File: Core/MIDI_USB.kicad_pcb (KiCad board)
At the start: 4 copper layers, 37.8 x 99.8 mm, 102 parts, among them J1 Conn_01x04, J10 AudioJack3_SwitchTR, J4 Conn_01x06, J5 USB_C_Receptacle_USB2.0, J6 Conn_02x08_Odd_Even, J7 AudioJack3_SwitchTR, J8 AudioJack3_SwitchTR, J9 AudioJack3_SwitchTR, Q3 SQ2361, Q4 2N7002, SW1 SW_Push_DPDT, U1 ATSAMD21G15B-A, U10 TLE9250V, U2 MIC2005-2YM5, U3 TUSB320, U4 TL072, U5 MIC5504-3.3YM5, U6 ES9023P, U7 PCM1808, U8 TL072, U9 MCP2517FD-xSL, Y1 20MHz

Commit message: Fix symbols
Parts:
- C35: value 22nF -> 4.7nF
- R28: value 10k -> 1k
- R4, R5: value 120 -> 56

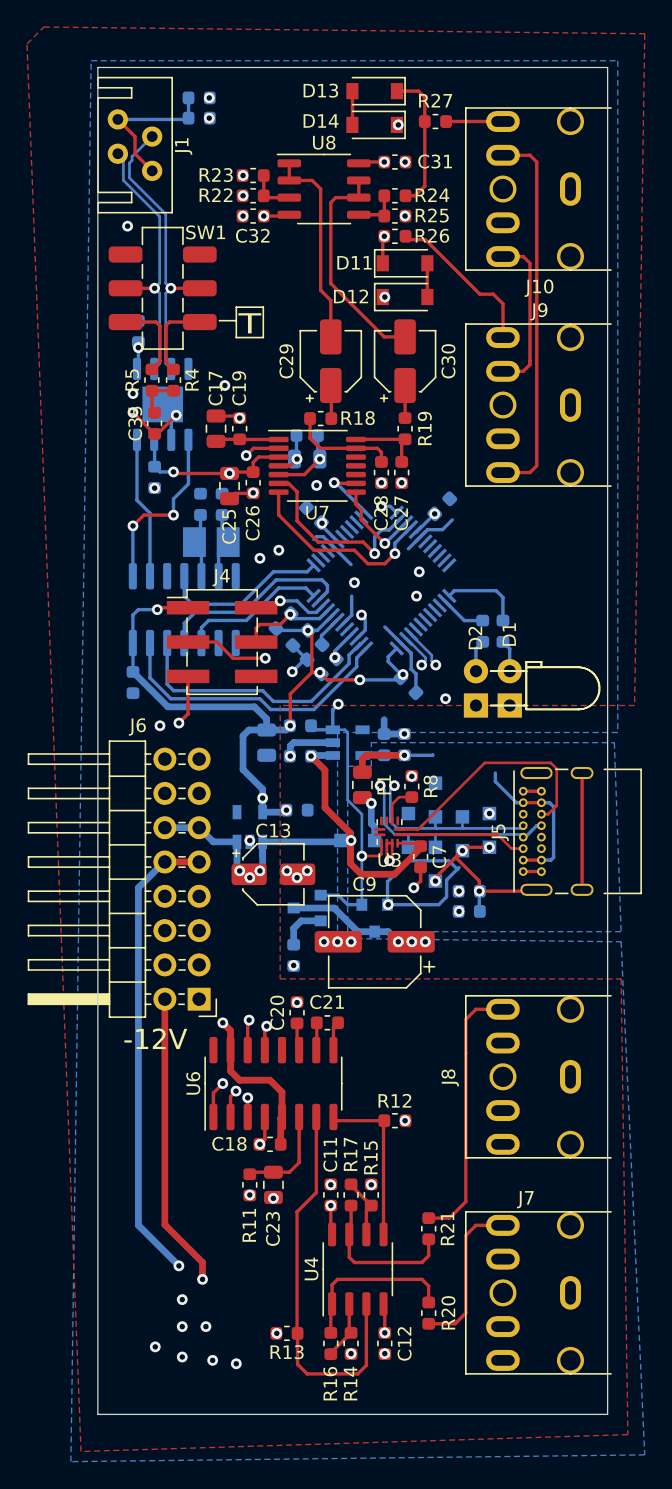
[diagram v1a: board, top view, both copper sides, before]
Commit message: Add custom footprints
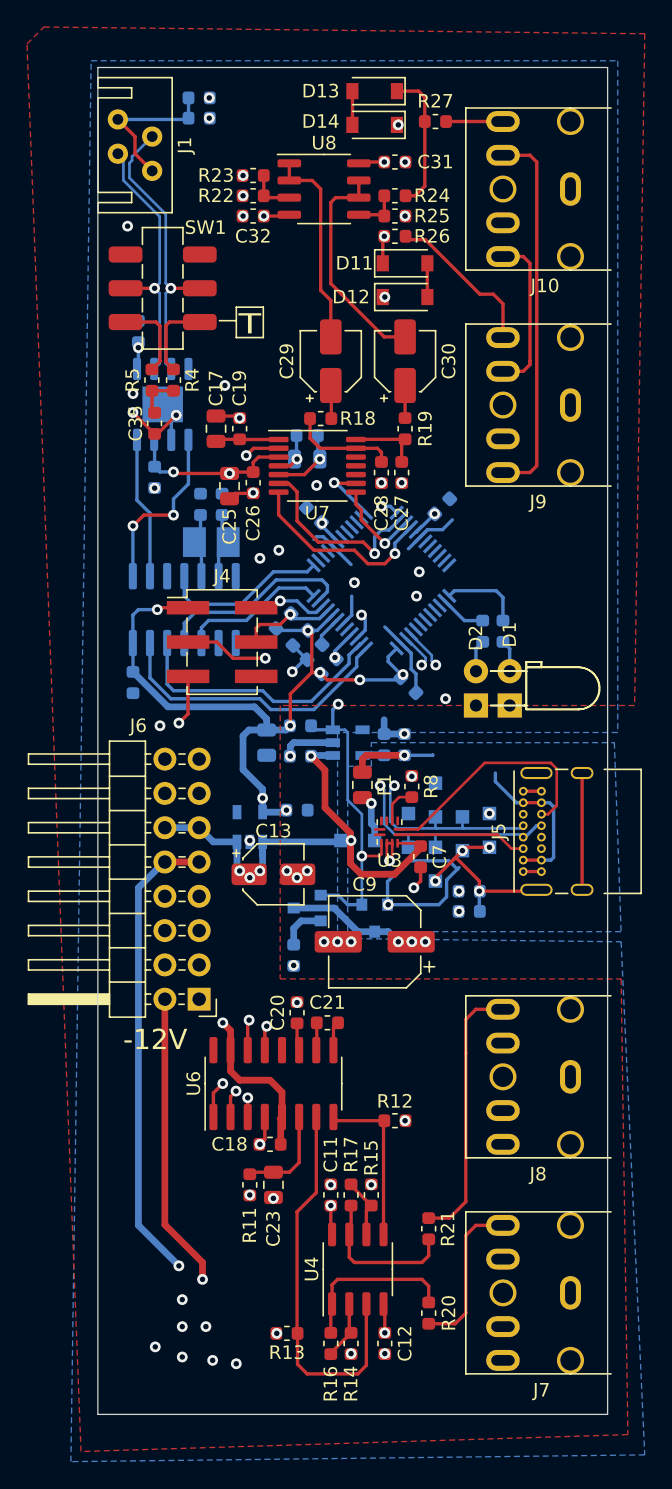
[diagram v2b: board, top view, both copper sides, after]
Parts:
- J1: footprint CustomLib:MicroMatch_04_Angled -> Custom_FP:MicroMatch_04_Angled
- J10, J7, J8, J9: footprint CustomLib:STX3100_Angled_3.5mm -> Custom_FP:STX3100_Angled_3.5mm
- J5: footprint CustomLib:USB_C_Receptacle_GCT_USB4085_Slimmed -> Custom_FP:USB_C_Receptacle_GCT_USB4085_Slimmed
- SW1: footprint CustomLib:SlideDPDT_JS202011 -> Custom_FP:SlideDPDT_JS202011
- Y1: footprint CustomLib:Crystal_2pin_2.0x2.5mm -> Custom_FP:Crystal_2pin_2.0x2.5mm
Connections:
- J10 pad RN: (no net) -> Net-(J10-PadRN)
- J4 pad 6: (no net) -> Net-(J4-Pad6)
- J5 pad A8: (no net) -> Net-(J5-PadA8)
- J5 pad B8: (no net) -> Net-(J5-PadB8)
- J6 pad 13: (no net) -> Net-(J6-Pad13)
- J6 pad 14: (no net) -> Net-(J6-Pad14)
- J6 pad 15: (no net) -> Net-(J6-Pad15)
- J6 pad 16: (no net) -> Net-(J6-Pad16)
- J7 pad R: (no net) -> Net-(J7-PadR)
- J7 pad RN: (no net) -> Net-(J7-PadRN)
- J7 pad TN: (no net) -> Net-(J7-PadTN)
- J8 pad R: (no net) -> Net-(J8-PadR)
- J8 pad RN: (no net) -> Net-(J8-PadRN)
- J8 pad TN: (no net) -> Net-(J8-PadTN)
- J9 pad RN: (no net) -> Net-(J9-PadRN)
- SW1 pad 3: (no net) -> Net-(SW1-Pad3)
- SW1 pad 6: (no net) -> Net-(SW1-Pad6)
- U1 pad 10: (no net) -> Net-(U1-Pad10)
- U1 pad 11: (no net) -> Net-(U1-Pad11)
- U1 pad 19: (no net) -> Net-(U1-Pad19)
- U1 pad 2: (no net) -> Net-(U1-Pad2)
- U1 pad 20: (no net) -> Net-(U1-Pad20)
- U1 pad 21: (no net) -> Net-(U1-Pad21)
- U1 pad 22: (no net) -> Net-(U1-Pad22)
- U1 pad 23: (no net) -> Net-(U1-Pad23)
- U1 pad 24: (no net) -> Net-(U1-Pad24)
- U1 pad 27: (no net) -> Net-(U1-Pad27)
- U1 pad 28: (no net) -> Net-(U1-Pad28)
- U1 pad 29: (no net) -> Net-(U1-Pad29)
- U1 pad 3: (no net) -> Net-(U1-Pad3)
- U1 pad 30: (no net) -> Net-(U1-Pad30)
- U1 pad 31: (no net) -> Net-(U1-Pad31)
- U1 pad 32: (no net) -> Net-(U1-Pad32)
- U1 pad 4: (no net) -> Net-(U1-Pad4)
- U1 pad 41: (no net) -> Net-(U1-Pad41)
- U1 pad 7: (no net) -> Net-(U1-Pad7)
- U1 pad 8: (no net) -> Net-(U1-Pad8)
- U1 pad 9: (no net) -> Net-(U1-Pad9)
- U2 pad 4: (no net) -> Net-(U2-Pad4)
- U3 pad 3: (no net) -> Net-(U3-Pad3)
- U3 pad 5: (no net) -> Net-(U3-Pad5)
- U3 pad 6: (no net) -> Net-(U3-Pad6)
- U3 pad 7: (no net) -> Net-(U3-Pad7)
- U3 pad 8: (no net) -> Net-(U3-Pad8)
- U5 pad 4: (no net) -> Net-(U5-Pad4)
- U6 pad 16: (no net) -> Net-(U6-Pad16)
- U7 pad 10: (no net) -> Net-(U7-Pad10)
- U7 pad 11: (no net) -> Net-(U7-Pad11)
- U7 pad 12: (no net) -> Net-(U7-Pad12)
- U9 pad 3: (no net) -> Net-(U9-Pad3)
- U9 pad 8: (no net) -> Net-(U9-Pad8)
- U9 pad 9: (no net) -> Net-(U9-Pad9)

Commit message: Update to v1.1
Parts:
- removed C13: 3.3µF, Capacitor_SMD:CP_Elec_4x5.4
- removed C8: 1µF, Capacitor_SMD:C_0603_1608Metric
- removed C9: 120µF, Capacitor_SMD:CP_Elec_6.3x5.7
- removed D13, D14: 5V6, Diode_SMD:D_SOD-123
- removed F1: PSMF020X-2, Fuse:Fuse_0805_2012Metric
- removed Q4: 2N7002, Package_TO_SOT_SMD:SOT-23
- removed R27: 1k, Resistor_SMD:R_0603_1608Metric
- removed U2: MIC2005-2YM5, Package_TO_SOT_SMD:SOT-23-5
- removed U3: TUSB320, Package_DFN_QFN:Texas_X2QFN-12_1.6x1.6mm_P0.4mm
- added C39: 100nF, Capacitor_SMD:C_0603_1608Metric, B.Cu at (150.2, 99.7)
- added C40: 100nF, Capacitor_SMD:C_0603_1608Metric, B.Cu at (157.2, 99.6)
- added C41: 15pF, Capacitor_SMD:C_0603_1608Metric, B.Cu at (148.6, 120.6)
- added C42: 15pF, Capacitor_SMD:C_0603_1608Metric, B.Cu at (146.4, 122.8)
- added C43: 1µF, Capacitor_SMD:C_0603_1608Metric, F.Cu at (158.0, 141.2)
- added C44: 47µF, Capacitor_SMD:C_1210_3225Metric, F.Cu at (151.8, 141.8)
- added C45: 47µF, Capacitor_SMD:C_1210_3225Metric, F.Cu at (151.8, 145.0)
- added C46: 47µF, Capacitor_SMD:C_1210_3225Metric, F.Cu at (151.8, 148.2)
- added D3: SD103, Diode_SMD:D_SOD-323_HandSoldering, F.Cu at (152.0, 112.8)
- added D4: SD103, Diode_SMD:D_SOD-323_HandSoldering, F.Cu at (150.0, 112.8)
- added Q1: ZXMP3A13, Package_TO_SOT_SMD:SOT-23, B.Cu at (144.8, 152.0)
- added Q2: PMV88ENER, Package_TO_SOT_SMD:SOT-23, B.Cu at (145.2, 159.5)
- added Q5: ZXMP3A13, Package_TO_SOT_SMD:SOT-23, B.Cu at (144.8, 148.0)
- added Q6: MMBT3904, Package_TO_SOT_SMD:SOT-23, B.Cu at (148.8, 152.5)
- added R29: 1M, Resistor_SMD:R_0603_1608Metric, B.Cu at (151.5, 154.5)
- added R30: 100k, Resistor_SMD:R_0603_1608Metric, B.Cu at (149.0, 149.5)
- added SW2: SW_SPST, Button_Switch_THT:SW_Tactile_SPST_Angled_PTS645Vx58-2LFS, F.Cu at (167.8, 124.9)
- added SW4: SW_SPST, Button_Switch_SMD:SW_SPST_B3U-1000P, F.Cu at (140.3, 126.7)
- added U11: CAT250640VI, Package_SO:SOIC-8_3.9x4.9mm_P1.27mm, B.Cu at (148.2, 105.0)
- added U12: APS1604M, Package_SO:SOIC-8_3.9x4.9mm_P1.27mm, B.Cu at (155.2, 105.0)
- added U13: ~, Package_SON:WSON-12-1EP_3x2mm_P0.5mm_EP1x2.65, F.Cu at (157.2, 144.1)
- added Y2: 32.768kHz, Crystal:Crystal_SMD_EuroQuartz_EQ161-2Pin_3.2x1.5mm_HandSoldering, B.Cu at (149.0, 123.2)
- C22, C24, R28: moved to F.Cu
- C29, C30: value 1µF -> 10µF bi-polar; footprint Capacitor_SMD:CP_Elec_4x5.4 -> Capacitor_SMD:CP_Elec_5x5.8
- D11, D12: value 5V6 -> SD103; footprint Diode_SMD:D_SOD-123 -> Diode_SMD:D_SOD-323_HandSoldering
- J5: footprint Custom_FP:USB_C_Receptacle_GCT_USB4085_Slimmed -> Connector_USB:USB_C_Receptacle_HRO_TYPE-C-31-M-12
- Q3: value SQ2361 -> MMBT3904
- R16, R17: value 42k -> 27k
- R26: value 1k -> 10k; moved to B.Cu
- R4, R5: value 56 -> 62
- R6: value 10k -> 100k; moved to F.Cu
- R8: value 910k -> 100k
- R9: value 470 -> 100k
- U1: value ATSAMD21G15B-A -> ATSAMD21G17D-A
- moved R26 19.7 mm to (161.0, 121.5), turned to -135 degrees
- moved R9 16.2 mm to (154.2, 141.2), turned to 0 degrees
- moved Q3 14.8 mm to (152.2, 138.5), turned to 90 degrees
- moved C20 12.0 mm to (158.0, 166.5), turned to 0 degrees
- moved C21 10.6 mm to (157.2, 168.8), turned to 90 degrees
- moved R6 9.22 mm to (155.0, 145.0), turned to -90 degrees
- moved D11 8.10 mm to (154.5, 112.8), turned to 90 degrees
- moved R22 7.28 mm to (146.5, 92.8), turned to 180 degrees
- moved R19 7.02 mm to (155.2, 110.0), turned to 180 degrees
- moved C7 6.96 mm to (155.0, 142.0), turned to 90 degrees
- moved U6 6.82 mm to (152.8, 164.5), turned to 0 degrees
- moved C30 6.77 mm to (156.2, 105.2)
- moved C29 6.75 mm to (150.2, 105.2)
- moved R18 6.49 mm to (151.2, 110.0), turned to 0 degrees
- moved C23 6.39 mm to (147.3, 166.8), turned to 180 degrees
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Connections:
- net MIDIBUS+ renamed M2IDI+
- net MIDIBUS- renamed M2IDI-
- net Net-(U1-Pad41) renamed PROG
- net SPI_SS renamed CAN_SS
- C11 pad 2: GNDA -> GND
- C12 pad 1: GNDA -> GND
- C17 pad 2: GNDA -> GND
- C18 pad 2: GNDA -> GND
- C19 pad 2: GNDA -> GND
- C20 pad 2: GNDA -> GND
- C23 pad 2: GNDA -> GND
- C25 pad 2: GNDA -> GND
- C26 pad 2: GNDA -> GND
- C27 pad 1: Net-(C27-Pad1) -> Net-(D11-A)
- C27 pad 2: GNDA -> GND
- C28 pad 2: GNDA -> GND
- C31 pad 2: GNDA -> GND
- C32 pad 1: GNDA -> GND
- D10 pad 2: Net-(D10-Pad2) -> VBUS
- D11 pad 1: Net-(D11-Pad1) -> +5V
- D11 pad 2: Net-(D11-Pad2) -> Net-(D11-A)
- D12 pad 1: GNDA -> Net-(D11-A)
- D12 pad 2: Net-(D11-Pad2) -> GND
- J10 pad RN: Net-(J10-PadRN) -> unconnected-(J10-PadRN)
- J10 pad S: GNDA -> GND
- J10 pad TN: Net-(J10-PadTN) -> unconnected-(J10-PadTN)
- J4 pad 6: Net-(J4-Pad6) -> unconnected-(J4-Pin_6-Pad6)
- J5 pad A8: Net-(J5-PadA8) -> unconnected-(J5-SBU1-PadA8)
- J5 pad B8: Net-(J5-PadB8) -> unconnected-(J5-SBU2-PadB8)
- J6 pad 1: -VDC -> Net-(J6-Pin_1)
- J6 pad 10: +VDC -> Net-(J6-Pin_10)
- J6 pad 11: +5V -> Net-(J6-Pin_11)
- J6 pad 12: +5V -> Net-(J6-Pin_11)
- J6 pad 13: Net-(J6-Pad13) -> unconnected-(J6-Pin_13-Pad13)
- J6 pad 14: Net-(J6-Pad14) -> unconnected-(J6-Pin_14-Pad14)
- J6 pad 15: Net-(J6-Pad15) -> unconnected-(J6-Pin_15-Pad15)
- J6 pad 16: Net-(J6-Pad16) -> unconnected-(J6-Pin_16-Pad16)
- J6 pad 2: -VDC -> Net-(J6-Pin_1)
- J6 pad 5: GNDA -> GND
- J6 pad 6: GNDA -> GND
- J6 pad 9: +VDC -> Net-(J6-Pin_10)
- J7 pad R: Net-(J7-PadR) -> unconnected-(J7-PadR)
- J7 pad RN: Net-(J7-PadRN) -> unconnected-(J7-PadRN)
- J7 pad S: GNDA -> GND
- J7 pad TN: Net-(J7-PadTN) -> unconnected-(J7-PadTN)
- J8 pad R: Net-(J8-PadR) -> unconnected-(J8-PadR)
- J8 pad RN: Net-(J8-PadRN) -> unconnected-(J8-PadRN)
- J8 pad S: GNDA -> GND
- J8 pad TN: Net-(J8-PadTN) -> unconnected-(J8-PadTN)
- J9 pad R: Net-(J10-PadTN) -> unconnected-(J9-PadR)
- J9 pad RN: Net-(J9-PadRN) -> unconnected-(J9-PadRN)
- J9 pad S: GNDA -> GND
- Q3 pad 1: USB_ID -> Net-(Q3-B)
- Q3 pad 2: VBUS -> GND
- Q3 pad 3: Net-(C9-Pad1) -> Net-(Q3-C)
- R11 pad 2: GNDA -> GND
- R12 pad 2: GNDA -> GND
- R13 pad 2: GNDA -> GND
- R14 pad 2: GNDA -> GND
- R15 pad 2: GNDA -> GND
- R19 pad 2: Net-(C27-Pad1) -> Net-(D11-A)
- R22 pad 1: Net-(D11-Pad1) -> Net-(J9-PadT)
- R22 pad 2: Net-(R22-Pad2) -> Net-(U8A--)
- R23 pad 1: Net-(R22-Pad2) -> Net-(U8A--)
- R23 pad 2: GNDA -> Net-(C29-Pad2)
- R24 pad 1: Net-(D13-Pad1) -> Net-(J10-PadT)
- R24 pad 2: Net-(R24-Pad2) -> Net-(U8B--)
- R25 pad 1: Net-(R24-Pad2) -> Net-(U8B--)
- R25 pad 2: GNDA -> Net-(C30-Pad2)
- R26 pad 1: Net-(J9-PadT) -> +3V3
- R26 pad 2: Net-(D11-Pad1) -> IO_BUTT
- R6 pad 1: +3V3 -> +5V
- R7 pad 1: VBUS -> +3V3
- R7 pad 2: GND -> Net-(Q3-C)
- R8 pad 1: VBUS -> Net-(U13-REF)
- R8 pad 2: Net-(R8-Pad2) -> GND
- R9 pad 1: Net-(Q4-Pad2) -> Net-(Q3-B)
- R9 pad 2: GND -> USB_ID
- SW1 pad 3: Net-(SW1-Pad3) -> unconnected-(SW1-C-Pad3)
- SW1 pad 6: Net-(SW1-Pad6) -> unconnected-(SW1-C-Pad6)
- U1 pad 1: CAN_INT -> Net-(U1-PA00)
- U1 pad 10: Net-(U1-Pad10) -> unconnected-(U1-PA05-Pad10)
- U1 pad 11: Net-(U1-Pad11) -> EEPROM_SS
- U1 pad 19: Net-(U1-Pad19) -> unconnected-(U1-PB10-Pad19)
- U1 pad 20: Net-(U1-Pad20) -> IO_BUTT
- U1 pad 21: Net-(U1-Pad21) -> SPI2_MOSI
- U1 pad 22: Net-(U1-Pad22) -> SPI2_SCK
- U1 pad 23: Net-(U1-Pad23) -> RAM_SS
- U1 pad 24: Net-(U1-Pad24) -> SPI2_MISO
- U1 pad 27: Net-(U1-Pad27) -> unconnected-(U1-PA18-Pad27)
- U1 pad 28: Net-(U1-Pad28) -> unconnected-(U1-PA19-Pad28)
- U1 pad 29: Net-(U1-Pad29) -> unconnected-(U1-PA20-Pad29)
- U1 pad 3: Net-(U1-Pad3) -> CAN_INT
- U1 pad 30: Net-(U1-Pad30) -> unconnected-(U1-PA21-Pad30)
- U1 pad 31: Net-(U1-Pad31) -> unconnected-(U1-PA22-Pad31)
- U1 pad 32: Net-(U1-Pad32) -> unconnected-(U1-PA23-Pad32)
- U1 pad 39: USB_ID -> Net-(Q3-C)
- U1 pad 4: Net-(U1-Pad4) -> unconnected-(U1-PA03-Pad4)
- U1 pad 7: Net-(U1-Pad7) -> unconnected-(U1-PB08-Pad7)
- U1 pad 8: Net-(U1-Pad8) -> unconnected-(U1-PB09-Pad8)
- U1 pad 9: Net-(U1-Pad9) -> unconnected-(U1-PA04-Pad9)
- U5 pad 4: Net-(U5-Pad4) -> unconnected-(U5-NC-Pad4)
- U6 pad 12: GNDA -> GND
- U6 pad 16: Net-(U6-Pad16) -> unconnected-(U6-ZD-Pad16)
- U6 pad 4: GNDA -> GND
- U7 pad 10: Net-(U7-Pad10) -> unconnected-(U7-MD0-Pad10)
- U7 pad 11: Net-(U7-Pad11) -> unconnected-(U7-MD1-Pad11)
- U7 pad 12: Net-(U7-Pad12) -> unconnected-(U7-FMT-Pad12)
- U7 pad 14: Net-(C27-Pad1) -> Net-(D11-A)
- U7 pad 2: GNDA -> GND
- U8 pad 2: Net-(C29-Pad2) -> Net-(U8A--)
- U8 pad 3: Net-(R22-Pad2) -> GND
- U8 pad 5: Net-(R24-Pad2) -> GND
- U8 pad 6: Net-(C30-Pad2) -> Net-(U8B--)
- U9 pad 3: Net-(U9-Pad3) -> unconnected-(U9-CLKO/SOF-Pad3)
- U9 pad 8: Net-(U9-Pad8) -> unconnected-(U9-~{INT1}/GPIO1-Pad8)
- U9 pad 9: Net-(U9-Pad9) -> unconnected-(U9-~{INT0}/GPIO0/XSTBY-Pad9)
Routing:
- net +3V3: track 166.5 -> 230.1 mm, vias 13 -> 17
- net SPI2_MISO: track 0.00 -> 39.8 mm, vias 0 -> 2
- net SPI2_SCK: track 0.00 -> 39.4 mm
- net SPI2_MOSI: track 0.00 -> 37.4 mm
- net Net-(J10-PadTN): track 27.9 -> 0.00 mm
- net VBUS: track 34.7 -> 8.66 mm, vias 4 -> 2
- net RAM_SS: track 0.00 -> 21.4 mm
- net USB_ID: track 33.3 -> 15.8 mm, vias 3 -> 1
- net Net-(Q3-C): track 0.00 -> 16.3 mm, vias 0 -> 2
- net EEPROM_SS: track 0.00 -> 15.5 mm
- net Net-(J9-PadT): track 11.7 -> 26.3 mm, vias 0 -> 1
- net Net-(D11-Pad1): track 14.0 -> 0.00 mm, vias 2 -> 0
- net Net-(D11-A): track 0.00 -> 12.5 mm
- net +VDC: track 113.0 -> 101.2 mm, vias 3 -> 5
- net Net-(Q5-G): track 0.00 -> 11.5 mm
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- added copper zone on F.Cu, net GND
- added copper zone on In1.Cu, net GND
- added copper zone on F.Cu, net VBUS
- removed copper zone on F.Cu, net GNDA
- removed copper zone on In1.Cu, net GNDA
- removed copper zone on In1.Cu, net VBUS
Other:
- net class Default removed
- net class Thin removed
- board text added: "MIDIBUS_USB V1.1 GuavTek"
- board text added: "RESET"
- board text removed: "MIDIBUS_USB V1.0 GuavTek"

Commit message: Minor fixes
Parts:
- moved R28 4.16 mm to (146.8, 127.5), turned to 180 degrees
- moved J9 1.35 mm to (168.0, 111.8)
- moved J7 0.65 mm to (168.0, 181.2)
- moved J8 0.65 mm to (168.0, 166.8)
- moved SW2 0.18 mm to (167.8, 124.7)
- moved J5 0.09 mm to (168.6, 146.8)
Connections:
- R22 pad 1: Net-(J9-PadT) -> Net-(J10-PadT)
- R24 pad 1: Net-(J10-PadT) -> Net-(J9-PadT)
- U6 pad 7: Net-(U4A-+) -> Net-(U4B-+)
- U6 pad 8: Net-(U4B-+) -> Net-(U4A-+)
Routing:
- net Net-(J9-PadT): track 26.3 -> 13.0 mm
- net Net-(J10-PadT): track 10.9 -> 15.9 mm, vias 0 -> 1
- net +3V3: track 230.1 -> 234.7 mm
- net SWCLK: track 11.5 -> 13.0 mm
- net Net-(D3-A): track 13.9 -> 14.9 mm, vias 0 -> 2
- net Net-(J10-PadR): track 10.1 -> 10.9 mm
- net Net-(D11-A): track 12.5 -> 13.2 mm, vias 0 -> 2
- net SWDIO: track 7.46 -> 8.18 mm
- net Net-(J7-PadT): track 12.6 -> 11.8 mm
- net Net-(U4A-+): track 30.8 -> 30.1 mm
- net Net-(J8-PadT): track 17.0 -> 17.5 mm
- net Net-(U4B-+): track 13.8 -> 14.4 mm
- net GND: track 51.1 -> 51.3 mm, vias 42 -> 56
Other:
- board text added: "M2IDI_USB V1.1 GuavTek"
- board text added: "VDD DIO RST CLK GND -"
- board text removed: "MIDIBUS_USB V1.1 GuavTek"
